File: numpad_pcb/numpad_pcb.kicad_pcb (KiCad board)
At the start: 2 copper layers, 76.2 x 103 mm, 25 parts, among them J1 numpad, U1 ProMicro

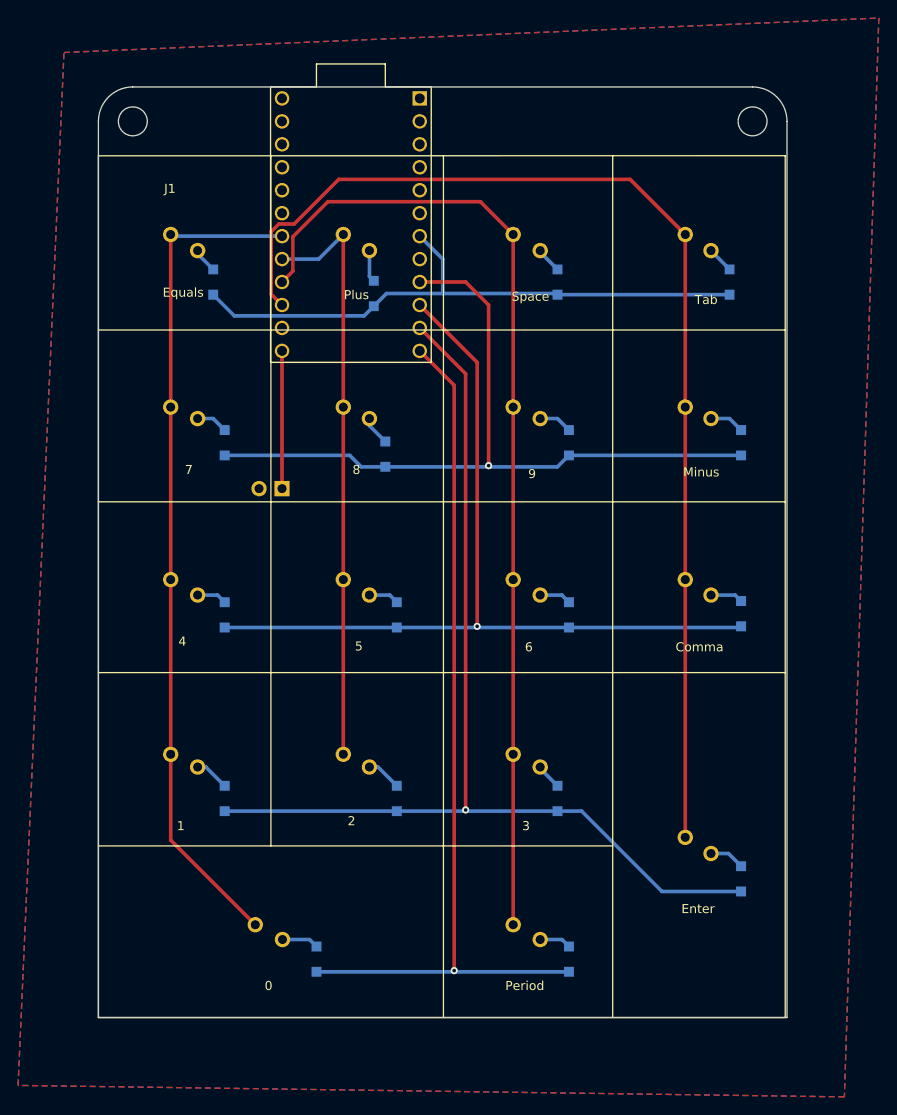
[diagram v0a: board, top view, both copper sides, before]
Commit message: fixed layout to allow for remapping to adm3a pinout
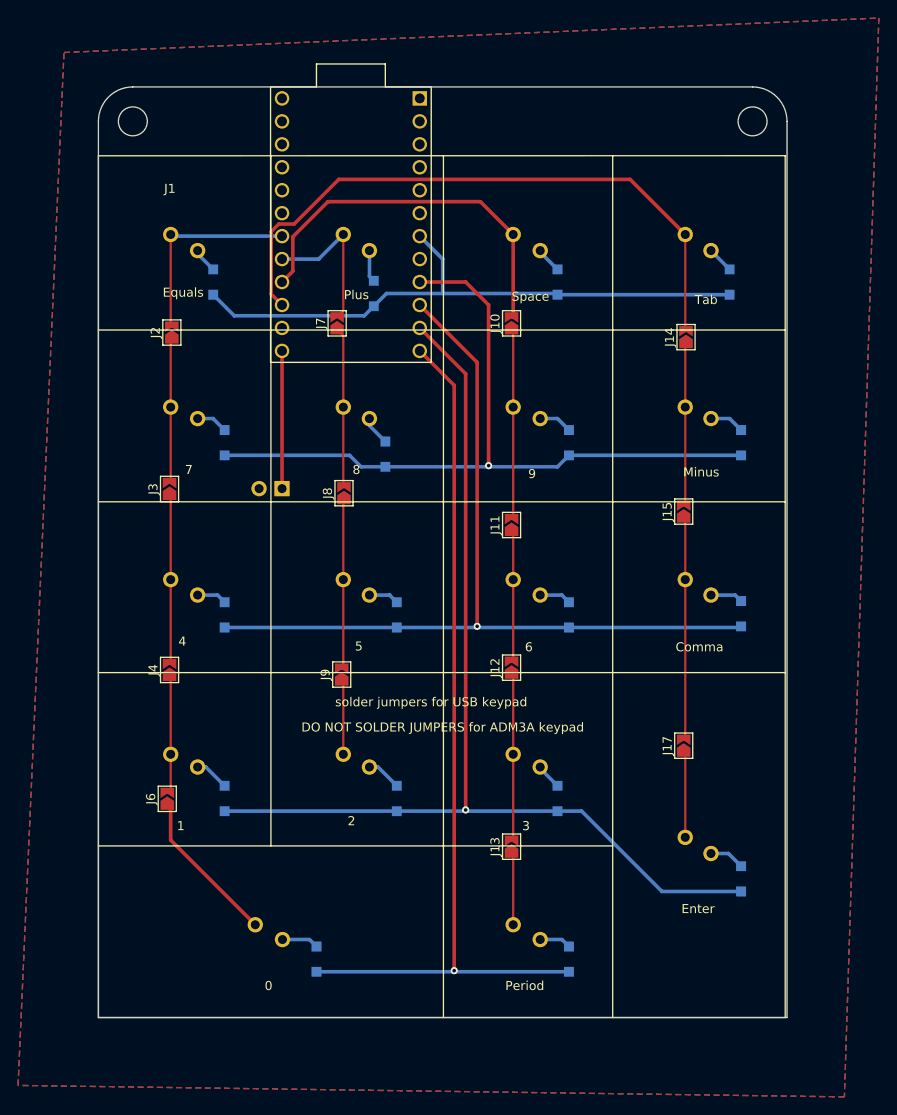
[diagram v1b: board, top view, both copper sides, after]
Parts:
- added J10: Conn_01x02, Jumper:SolderJumper-2_P1.3mm_Open_TrianglePad1.0x1.5mm, F.Cu at (154.9, 63.0)
- added J11: Conn_01x02, Jumper:SolderJumper-2_P1.3mm_Open_TrianglePad1.0x1.5mm, F.Cu at (154.9, 85.3)
- added J12: Conn_01x02, Jumper:SolderJumper-2_P1.3mm_Open_TrianglePad1.0x1.5mm, F.Cu at (154.9, 101.1)
- added J13: Conn_01x02, Jumper:SolderJumper-2_P1.3mm_Open_TrianglePad1.0x1.5mm, F.Cu at (154.9, 120.9)
- added J14: Conn_01x02, Jumper:SolderJumper-2_P1.3mm_Open_TrianglePad1.0x1.5mm, F.Cu at (174.2, 64.5)
- added J15: Conn_01x02, Jumper:SolderJumper-2_P1.3mm_Open_TrianglePad1.0x1.5mm, F.Cu at (174.0, 83.8)
- added J17: Conn_01x02, Jumper:SolderJumper-2_P1.3mm_Open_TrianglePad1.0x1.5mm, F.Cu at (174.0, 109.7)
- added J2: Conn_01x02, Jumper:SolderJumper-2_P1.3mm_Open_TrianglePad1.0x1.5mm, F.Cu at (117.3, 64.0)
- added J3: Conn_01x02, Jumper:SolderJumper-2_P1.3mm_Open_TrianglePad1.0x1.5mm, F.Cu at (117.1, 81.3)
- added J4: Conn_01x02, Jumper:SolderJumper-2_P1.3mm_Open_TrianglePad1.0x1.5mm, F.Cu at (117.1, 101.3)
- added J6: Conn_01x02, Jumper:SolderJumper-2_P1.3mm_Open_TrianglePad1.0x1.5mm, F.Cu at (116.8, 115.6)
- added J7: Conn_01x02, Jumper:SolderJumper-2_P1.3mm_Open_TrianglePad1.0x1.5mm, F.Cu at (135.6, 63.0)
- added J8: Conn_01x02, Jumper:SolderJumper-2_P1.3mm_Open_TrianglePad1.0x1.5mm, F.Cu at (136.4, 81.8)
- added J9: Conn_01x02, Jumper:SolderJumper-2_P1.3mm_Open_TrianglePad1.0x1.5mm, F.Cu at (136.1, 101.9)
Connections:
- J1 pad 11: /col2 -> Net-(J1-Pad11)
- J1 pad 13: /col3 -> Net-(J1-Pad13)
- J1 pad 15: /col4 -> Net-(J1-Pad15)
- J1 pad 17: /col1 -> Net-(J1-Pad17)
- J1 pad 19: /col2 -> Net-(J1-Pad19)
- J1 pad 21: /col3 -> Net-(J1-Pad21)
- J1 pad 23: /col4 -> Net-(J17-Pad2)
- J1 pad 25: /col1 -> Net-(J1-Pad25)
- J1 pad 27: /col2 -> Net-(J1-Pad27)
- J1 pad 29: /col3 -> Net-(J1-Pad29)
- J1 pad 31: /col4 -> Net-(J1-Pad31)
- J1 pad 33: /col1 -> Net-(J1-Pad33)
- J1 pad 35: /col3 -> Net-(J1-Pad35)
- J1 pad 9: /col1 -> Net-(J1-Pad9)
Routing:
- net /col1: track 92.7 -> 22.6 mm
- net /col3: track 109.4 -> 42.2 mm
- net /col4: track 126.1 -> 70.0 mm
- net /col2: track 65.4 -> 17.3 mm
- net Net-(J17-Pad2): track 0.00 -> 24.6 mm
- net Net-(J1-Pad13): track 0.00 -> 21.0 mm
- net Net-(J1-Pad19): track 0.00 -> 18.7 mm
- net Net-(J1-Pad17): track 0.00 -> 18.7 mm
- net Net-(J1-Pad29): track 0.00 -> 18.5 mm
- net Net-(J1-Pad15): track 0.00 -> 18.0 mm
- net Net-(J1-Pad11): track 0.00 -> 17.7 mm
- net Net-(J1-Pad33): track 0.00 -> 17.2 mm
- net Net-(J1-Pad9): track 0.00 -> 16.0 mm
- net Net-(J1-Pad21): track 0.00 -> 14.5 mm
- net Net-(J1-Pad25): track 0.00 -> 13.0 mm
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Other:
- board text added: "DO NOT SOLDER JUMPERS for ADM3A keypad"
- board text added: "solder jumpers for USB keypad"

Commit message: generated gerbers
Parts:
- moved J8 2.90 mm to (136.5, 84.7)
- moved J10 2.79 mm to (154.9, 65.8)
- moved J7 2.67 mm to (136.4, 65.6)
- moved J9 2.06 mm to (136.1, 99.8)
- moved J13 2.02 mm to (155.1, 122.9)
- moved J2 2.01 mm to (117.3, 66.0)
- moved J4 1.52 mm to (116.7, 99.9)
- moved J15 1.40 mm to (174.1, 85.2)
- moved J12 1.35 mm to (154.6, 99.8)
- moved J14 1.19 mm to (174.3, 65.7)
- moved J3 0.58 mm to (117.2, 80.7)
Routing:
- net Net-(J1-Pad19): track 18.7 -> 13.8 mm
- net Net-(J1-Pad29): track 18.5 -> 21.9 mm
- net /col3: track 42.2 -> 45.0 mm
- net Net-(J1-Pad13): track 21.0 -> 18.2 mm
- net Net-(J1-Pad9): track 16.0 -> 13.3 mm
- net /col2: track 17.3 -> 19.6 mm
- net Net-(J1-Pad35): track 7.99 -> 5.91 mm
- net Net-(J1-Pad27): track 8.17 -> 10.2 mm
- net /col1: track 22.6 -> 24.6 mm
- net Net-(J1-Pad25): track 13.0 -> 14.6 mm
- net Net-(J17-Pad2): track 24.6 -> 23.1 mm
- net /col4: track 70.0 -> 71.2 mm
- net Net-(J1-Pad21): track 14.5 -> 13.3 mm
- net Net-(J1-Pad17): track 18.7 -> 17.9 mm

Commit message: tweaked silk, added todo for upgraded layout, added config
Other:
- board text added: "QMK capable pcb for electronics goldmine numpad"
- board text removed: "QMK capable pcv for electronics goldmine numpad pcb"
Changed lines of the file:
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@@
     (effects (font (size 1 1) (thickness 0.15)) (justify mirror))
   )
-  (gr_text "QMK capable pcv for electronics goldmine numpad pcb" (at 146.05 101.6) (layer "B.SilkS")
+  (gr_text "QMK capable pcb for electronics goldmine numpad" (at 146.05 101.6) (layer "B.SilkS")
     (effects (font (size 1 1) (thickness 0.15)) (justify mirror))
   )

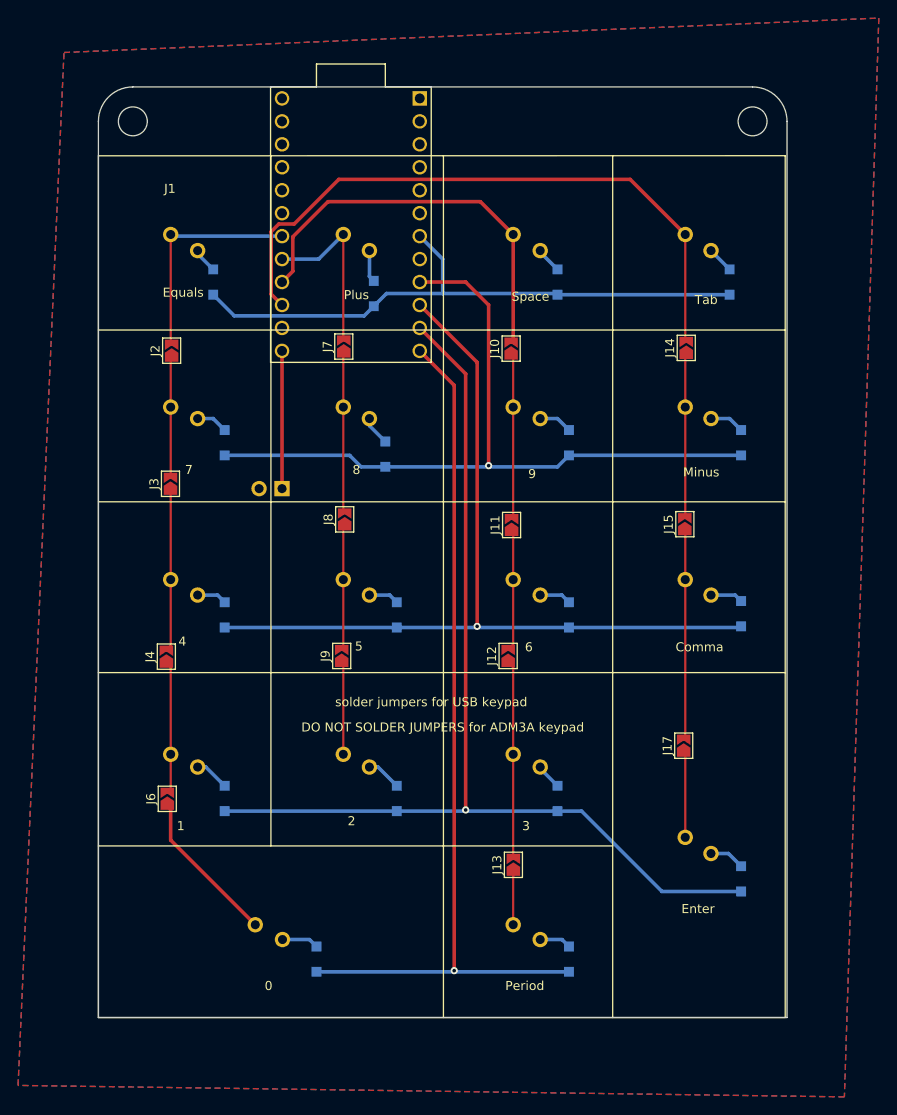
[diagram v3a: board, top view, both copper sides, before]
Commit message: moved jumpers to the back
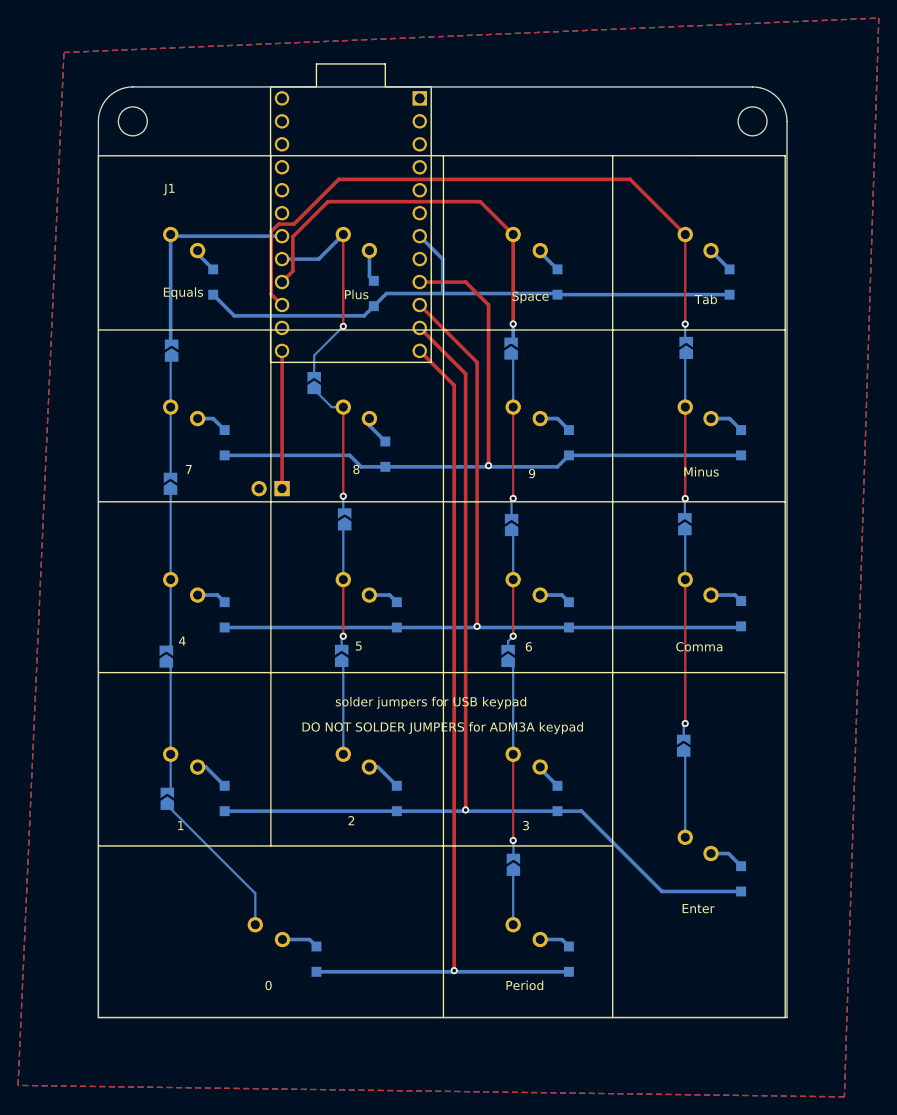
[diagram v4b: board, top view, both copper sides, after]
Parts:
- J10, J11, J12, J13, J14, J15, J17, J2, J3, J4, J6, J7, J8, J9: moved to B.Cu
- moved J7 5.20 mm to (133.1, 69.6)
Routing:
- net /col2: track 19.6 -> 25.0 mm, vias 0 -> 1
- net Net-(J1-Pad11): track 17.8 -> 15.8 mm, vias 0 -> 1
- net Net-(J1-Pad29): vias 0 -> 1
- net Net-(J15-Pad1): vias 0 -> 1
- net Net-(J1-Pad13): vias 0 -> 1
- net Net-(J1-Pad21): vias 0 -> 1
- net Net-(J14-Pad1): vias 0 -> 1
- net Net-(J1-Pad19): vias 0 -> 1
- net /col4: vias 0 -> 1
- net /col3: vias 0 -> 1
